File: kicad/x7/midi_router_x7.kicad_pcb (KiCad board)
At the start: 2 copper layers, 160 x 80 mm, 130 parts, among them J1 DIN-5_180degree, J10 DIN-5_180degree, J11 Conn_02x03_Odd_Even, J12 DIN-5_180degree, J13 DIN-5_180degree, J14 DIN-5_180degree, J15 DIN-5_180degree, J16 USB_B, J2 DIN-5_180degree, J3 DIN-5_180degree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

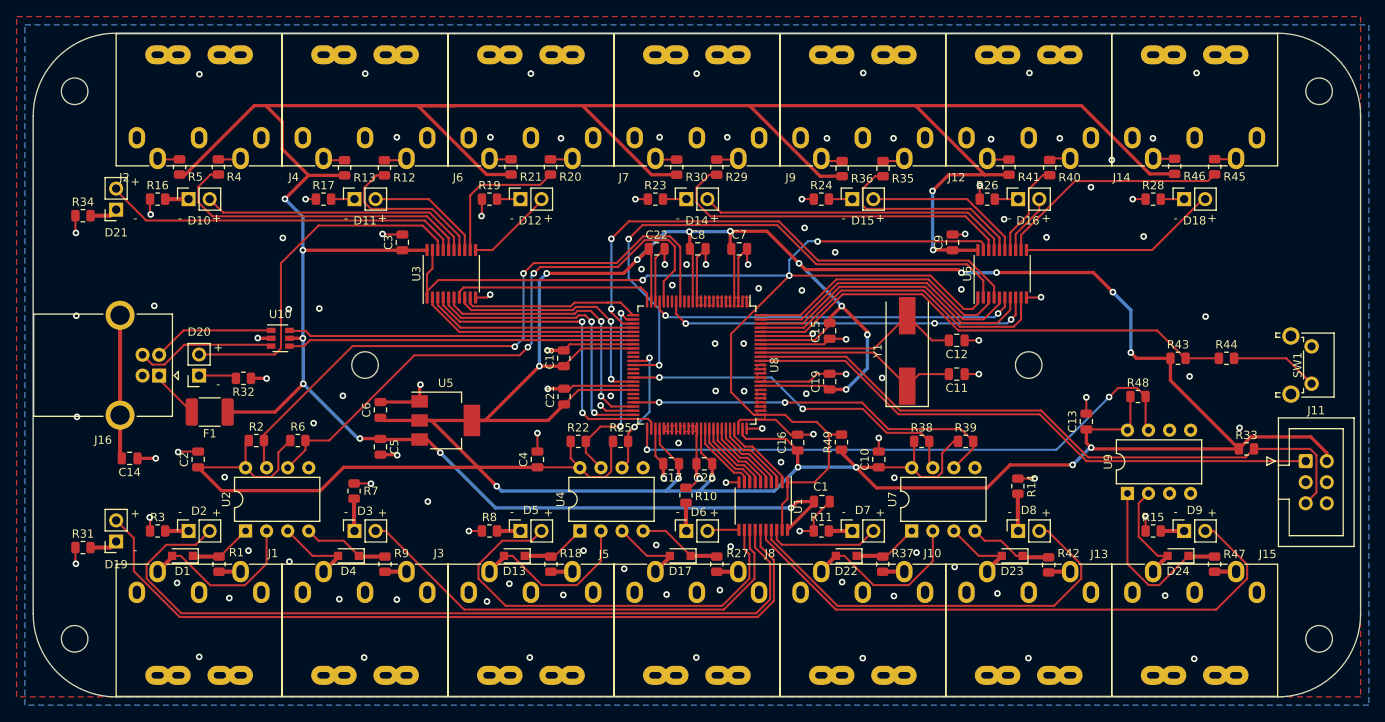
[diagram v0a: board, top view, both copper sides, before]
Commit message: Minor tracing fixes.
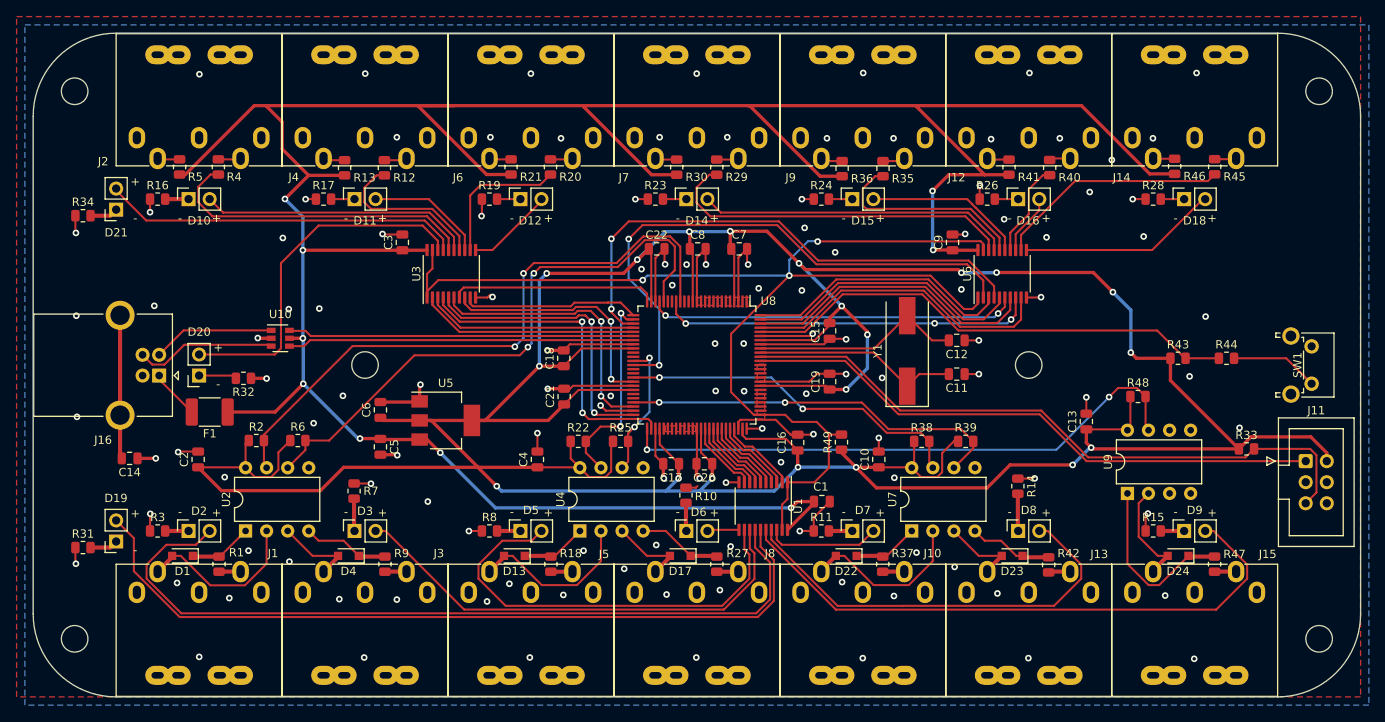
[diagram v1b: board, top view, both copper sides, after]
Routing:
- net GND: track 160.4 -> 160.3 mm, vias 122 -> 121
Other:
- board text added: "2021.07.29"
- board text removed: "2021.07.26"
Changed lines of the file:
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@@
     (thickness 1.6)
     (drawings 17)
-    (tracks 1137)
+    (tracks 1135)
     (zones 0)
     (modules 130)
@@
     (descr "standard DIN connector, 5 pins, midi")
     (tags "OOTDTY DIN 5-pins connector midi")
-    (fp_text reference J2 (at -1.5 4.8) (layer F.SilkS)
+    (fp_text reference J2 (at -4.0724 2.8634) (layer F.SilkS)
       (effects (font (size 1 1) (thickness 0.15)))
     )
@@
     (tags "TQFP QFP")
     (attr smd)
-    (fp_text reference U8 (at 0 -9.35 90) (layer F.SilkS)
+    (fp_text reference U8 (at -7.7218 -8.6154 180) (layer F.SilkS)
       (effects (font (size 1 1) (thickness 0.15)))
     )
@@
     (descr "Through hole straight socket strip, 1x02, 2.54mm pitch, single row (from Kicad 4.0.7), script generated")
     (tags "Through hole socket strip THT 1x02 2.54mm single row")
-    (fp_text reference D19 (at 0 -2.77) (layer F.SilkS)
+    (fp_text reference D19 (at 0.023 5.2174) (layer F.SilkS)
       (effects (font (size 1 1) (thickness 0.15)))
     )
@@
     (effects (font (size 1 1) (thickness 0.15)) (justify mirror))
   )
-  (gr_text 2021.07.26 (at 76.9112 132.6134) (layer B.SilkS)
+  (gr_text 2021.07.29 (at 76.9112 132.6134) (layer B.SilkS)
     (effects (font (size 1.2 1.4) (thickness 0.2)) (justify mirror))
   )
@@
   (segment (start 157.4292 110.5612) (end 159.197 112.329) (width 0.4) (layer F.Cu) (net 1) (status 10))
   (segment (start 157.4292 110.2087) (end 157.4292 110.5612) (width 0.4) (layer F.Cu) (net 1) (status 30))
-  (via (at 74.041 118.364) (size 0.8) (drill 0.4) (layers F.Cu B.Cu) (net 2))
-  (segment (start 74.0875 118.4105) (end 74.041 118.364) (width 0.25) (layer F.Cu) (net 2))
-  (segment (start 74.0875 120) (end 74.0875 118.4105) (width 0.25) (layer F.Cu) (net 2) (status 10))
   (via (at 65.151 123.952) (size 0.8) (drill 0.4) (layers F.Cu B.Cu) (net 2))
   (segment (start 65.0875 123.8885) (end 65.151 123.952) (width 0.25) (layer F.Cu) (net 2))
@@
   (segment (start 192.542 80) (end 192.532 80.01) (width 0.25) (layer F.Cu) (net 2))
   (segment (start 194.0875 80) (end 192.542 80) (width 0.25) (layer F.Cu) (net 2) (status 10))
-  (via (at 194.056 118.237) (size 0.8) (drill 0.4) (layers F.Cu B.Cu) (net 2))
-  (segment (start 194.0875 118.2685) (end 194.056 118.237) (width 0.25) (layer F.Cu) (net 2))
-  (segment (start 194.0875 120) (end 194.0875 118.2685) (width 0.25) (layer F.Cu) (net 2) (status 10))
   (via (at 180.721 113.665) (size 0.8) (drill 0.4) (layers F.Cu B.Cu) (net 2))
   (segment (start 180.6985 113.6875) (end 180.721 113.665) (width 0.25) (layer F.Cu) (net 2))
@@
   (segment (start 155.335 97.5) (end 156 96.835) (width 0.25) (layer F.Cu) (net 2) (status 20))
   (segment (start 147.6625 97.5) (end 155.335 97.5) (width 0.25) (layer F.Cu) (net 2) (status 10))
-  (segment (start 140 108.465702) (end 140 107.6625) (width 0.25) (layer F.Cu) (net 2) (status 20))
-  (segment (start 139.95 108.515702) (end 140 108.465702) (width 0.25) (layer F.Cu) (net 2))
-  (segment (start 139.95 111.9) (end 139.95 108.515702) (width 0.25) (layer F.Cu) (net 2) (status 10))
   (segment (start 135 110.95) (end 135.95 111.9) (width 0.25) (layer F.Cu) (net 2) (status 20))
   (segment (start 135 107.6625) (end 135 110.95) (width 0.25) (layer F.Cu) (net 2) (status 10))
@@
   (segment (start 141.05 87.837) (end 141.097 87.884) (width 0.25) (layer F.Cu) (net 2))
   (segment (start 141.05 86) (end 141.05 87.837) (width 0.25) (layer F.Cu) (net 2) (status 10))
-  (via (at 136.144 87.884) (size 0.8) (drill 0.4) (layers F.Cu B.Cu) (net 2))
-  (segment (start 136.1 87.84) (end 136.144 87.884) (width 0.25) (layer F.Cu) (net 2))
-  (segment (start 136.1 86) (end 136.1 87.84) (width 0.25) (layer F.Cu) (net 2) (status 10))
   (segment (start 124.689 97.5) (end 123.952 98.237) (width 0.25) (layer F.Cu) (net 2) (status 20))
   (segment (start 132.3375 97.5) (end 124.689 97.5) (width 0.25) (layer F.Cu) (net 2) (status 10))
@@
   (segment (start 135.95 113.598) (end 136.017 113.665) (width 0.4) (layer F.Cu) (net 2))
   (segment (start 135.95 111.9) (end 135.95 113.598) (width 0.4) (layer F.Cu) (net 2) (status 10))
-  (segment (start 138.684 114.7845) (end 139.2155 114.7845) (width 0.25) (layer F.Cu) (net 2) (status 30))
   (via (at 140.335 113.665) (size 0.8) (drill 0.4) (layers F.Cu B.Cu) (net 2))
   (segment (start 139.95 111.9) (end 139.95 113.28) (width 0.4) (layer F.Cu) (net 2) (status 10))
   (segment (start 139.95 113.28) (end 140.335 113.665) (width 0.4) (layer F.Cu) (net 2))
-  (segment (start 139.2155 114.7845) (end 140.335 113.665) (width 0.25) (layer F.Cu) (net 2) (status 10))
   (via (at 103.886 110.871) (size 0.8) (drill 0.4) (layers F.Cu B.Cu) (net 2))
   (segment (start 103.82 110.805) (end 103.886 110.871) (width 0.4) (layer F.Cu) (net 2))
@@
   (segment (start 132.3375 102.5) (end 132.334698 102.502802) (width 0.25) (layer F.Cu) (net 2) (status 30))
   (segment (start 114.7411 91.8625) (end 115.0874 91.5162) (width 0.25) (layer F.Cu) (net 2))
-  (via (at 115.0874 91.5162) (size 0.8) (drill 0.4) (layers F.Cu B.Cu) (net 2))
+  (via (at 115.3668 91.7956) (size 0.8) (drill 0.4) (layers F.Cu B.Cu) (net 2))
   (segment (start 113.325 91.8625) (end 114.7411 91.8625) (width 0.25) (layer F.Cu) (net 2) (status 10))
   (segment (start 87.0966 96.774) (end 87.0712 96.7486) (width 0.4) (layer F.Cu) (net 2))
@@
   (via (at 190.0174 75.2856) (size 0.8) (drill 0.4) (layers F.Cu B.Cu) (net 2))
   (via (at 152.9842 83.4644) (size 0.8) (drill 0.4) (layers F.Cu B.Cu) (net 2))
-  (via (at 187.5028 78.5622) (size 0.8) (drill 0.4) (layers F.Cu B.Cu) (net 2))
+  (via (at 187.3504 79.1464) (size 0.8) (drill 0.4) (layers F.Cu B.Cu) (net 2))
   (via (at 193.8528 84.5058) (size 0.8) (drill 0.4) (layers F.Cu B.Cu) (net 2))
   (via (at 156.6672 86.4108) (size 0.8) (drill 0.4) (layers F.Cu B.Cu) (net 2))
@@
   (segment (start 129.7736 103.5676) (end 129.6162 103.725) (width 0.25) (layer F.Cu) (net 2))
   (segment (start 129.7736 103.5) (end 129.7736 103.5676) (width 0.25) (layer F.Cu) (net 2))
-  (via (at 137.795 109.3978) (size 0.8) (drill 0.4) (layers F.Cu B.Cu) (net 2))
   (via (at 138.7602 87.884) (size 0.8) (drill 0.4) (layers F.Cu B.Cu) (net 2))
   (via (at 137.033 90.3732) (size 0.8) (drill 0.4) (layers F.Cu B.Cu) (net 2))
-  (segment (start 74.0875 81.76989) (end 74.168 81.85039) (width 0.25) (layer F.Cu) (net 2))
-  (via (at 74.168 81.85039) (size 0.8) (drill 0.4) (layers F.Cu B.Cu) (net 2))
-  (segment (start 74.0875 80) (end 74.0875 81.76989) (width 0.25) (layer F.Cu) (net 2) (status 10))
   (via (at 161.924998 108.7882) (size 0.8) (drill 0.4) (layers F.Cu B.Cu) (net 2))
   (segment (start 161.925 108.788202) (end 161.924998 108.7882) (width 0.25) (layer F.Cu) (net 2))
@@
   (via (at 171.8818 90.8812) (size 0.8) (drill 0.4) (layers F.Cu B.Cu) (net 2))
   (via (at 177.038 82.423) (size 0.8) (drill 0.4) (layers F.Cu B.Cu) (net 2))
+  (segment (start 140 108.465702) (end 140 107.6625) (width 0.25) (layer F.Cu) (net 2))
+  (segment (start 140 111.85) (end 140 108.465702) (width 0.25) (layer F.Cu) (net 2))
+  (segment (start 139.95 111.9) (end 140 111.85) (width 0.25) (layer F.Cu) (net 2))
+  (via (at 136.1694 87.8586) (size 0.8) (drill 0.4) (layers F.Cu B.Cu) (net 2))
+  (segment (start 136.1 87.7892) (end 136.1694 87.8586) (width 0.25) (layer F.Cu) (net 2))
+  (segment (start 136.1 86) (end 136.1 87.7892) (width 0.25) (layer F.Cu) (net 2))
+  (segment (start 139.8759 114.7845) (end 140.081 114.5794) (width 0.25) (layer F.Cu) (net 2))
+  (segment (start 138.684 114.7845) (end 139.8759 114.7845) (width 0.25) (layer F.Cu) (net 2))
+  (via (at 194.3608 117.9068) (size 0.8) (drill 0.4) (layers F.Cu B.Cu) (net 2))
+  (segment (start 194.0875 120) (end 194.0875 118.1801) (width 0.25) (layer F.Cu) (net 2))
+  (segment (start 194.0875 118.1801) (end 194.3608 117.9068) (width 0.25) (layer F.Cu) (net 2))
+  (via (at 74.1172 117.9322) (size 0.8) (drill 0.4) (layers F.Cu B.Cu) (net 2))
+  (segment (start 74.0875 120) (end 74.0875 117.9619) (width 0.25) (layer F.Cu) (net 2))
+  (segment (start 74.0875 117.9619) (end 74.1172 117.9322) (width 0.25) (layer F.Cu) (net 2))
+  (via (at 74.0875 81.580498) (size 0.8) (drill 0.4) (layers F.Cu B.Cu) (net 2))
+  (segment (start 74.0875 80) (end 74.0875 81.580498) (width 0.25) (layer F.Cu) (net 2))
   (segment (start 79.3375 123.0875) (end 79.25 123) (width 0.5) (layer F.Cu) (net 3) (status 30))
   (segment (start 82.4 123.0875) (end 79.3375 123.0875) (width 0.5) (layer F.Cu) (net 3) (status 30))

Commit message: Minor tweaks.
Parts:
- D10, D11, D12, D14, D15, D16, D18, D21: value LED -> L-383GDT
- D19, D2, D3, D5, D6, D7, D8, D9: value LED -> L-383YDT
- D20: value LED -> L-383ID
- R2, R22, R25, R38, R39, R48, R6: value 470 -> 220
- U2, U4, U7, U9: value HCPL2730 -> HCPL2631

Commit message: x7 KiCad upgrade
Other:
- net class Default removed
- net class Short&Fat removed
- net class Thick removed
